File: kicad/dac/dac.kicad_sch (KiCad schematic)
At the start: 41 parts, among them J1 USB_C_Receptacle_USB2.0, J2 Conn_01x03, J3 Conn_01x03, J4 AudioJack3, P1 Conn_WallPlug_Earth, T1 Transformer_SP_2S, U2 PCM2704/4C/5/5C, Y1 12MHz±0.05%

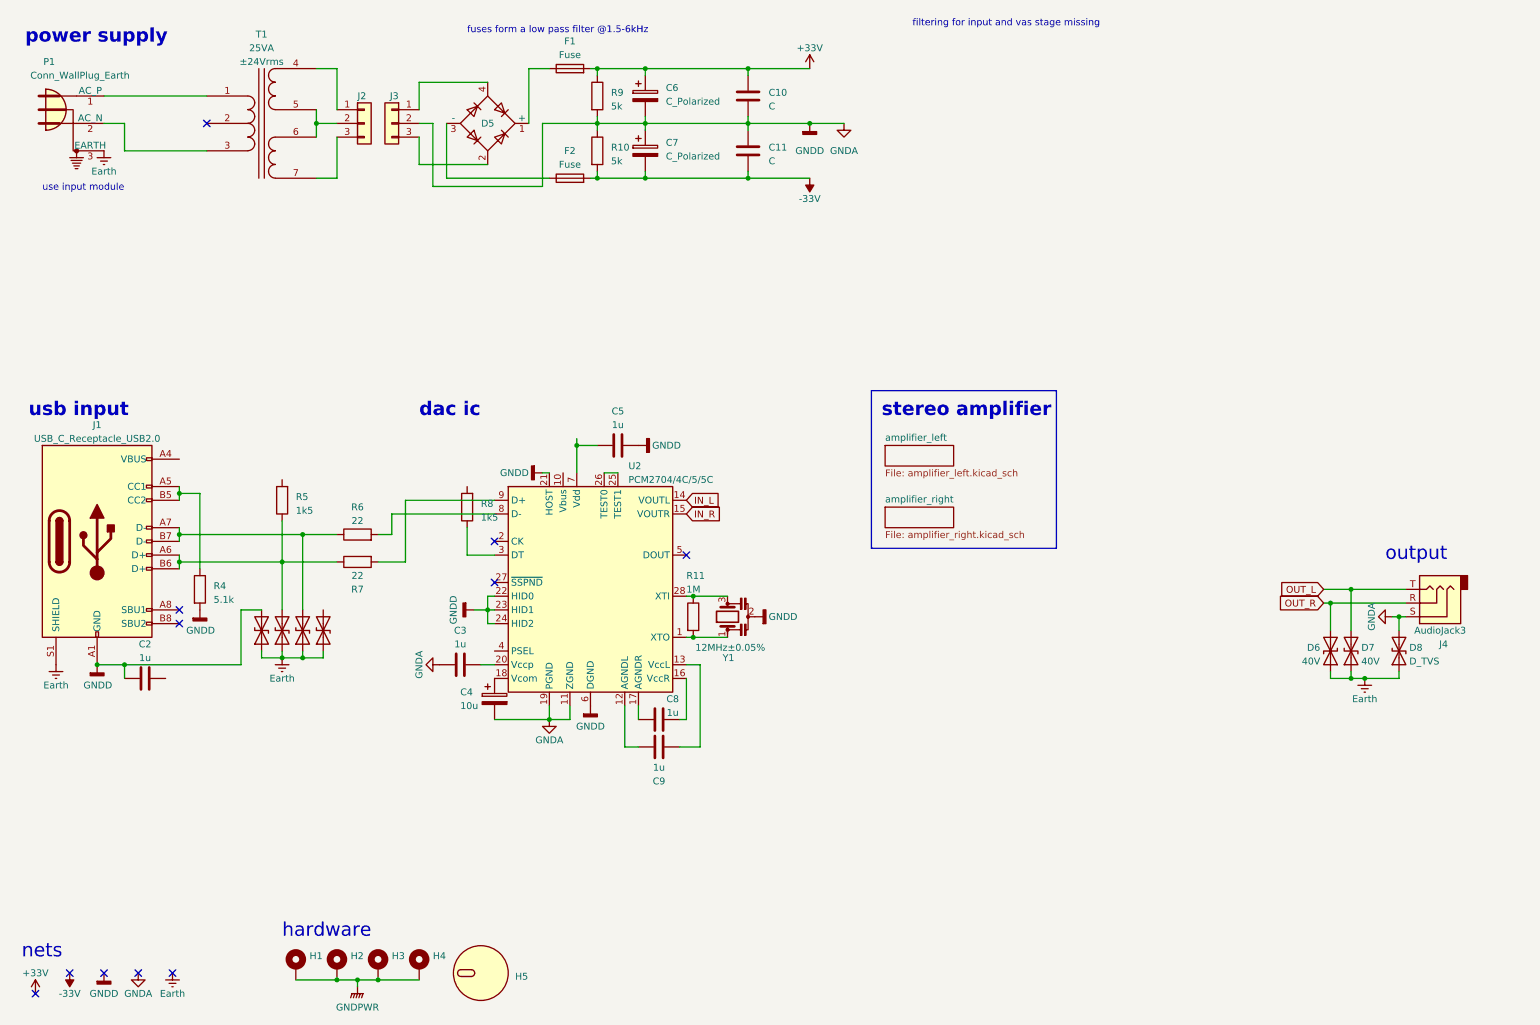
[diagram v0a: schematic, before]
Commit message: split power supply to different board
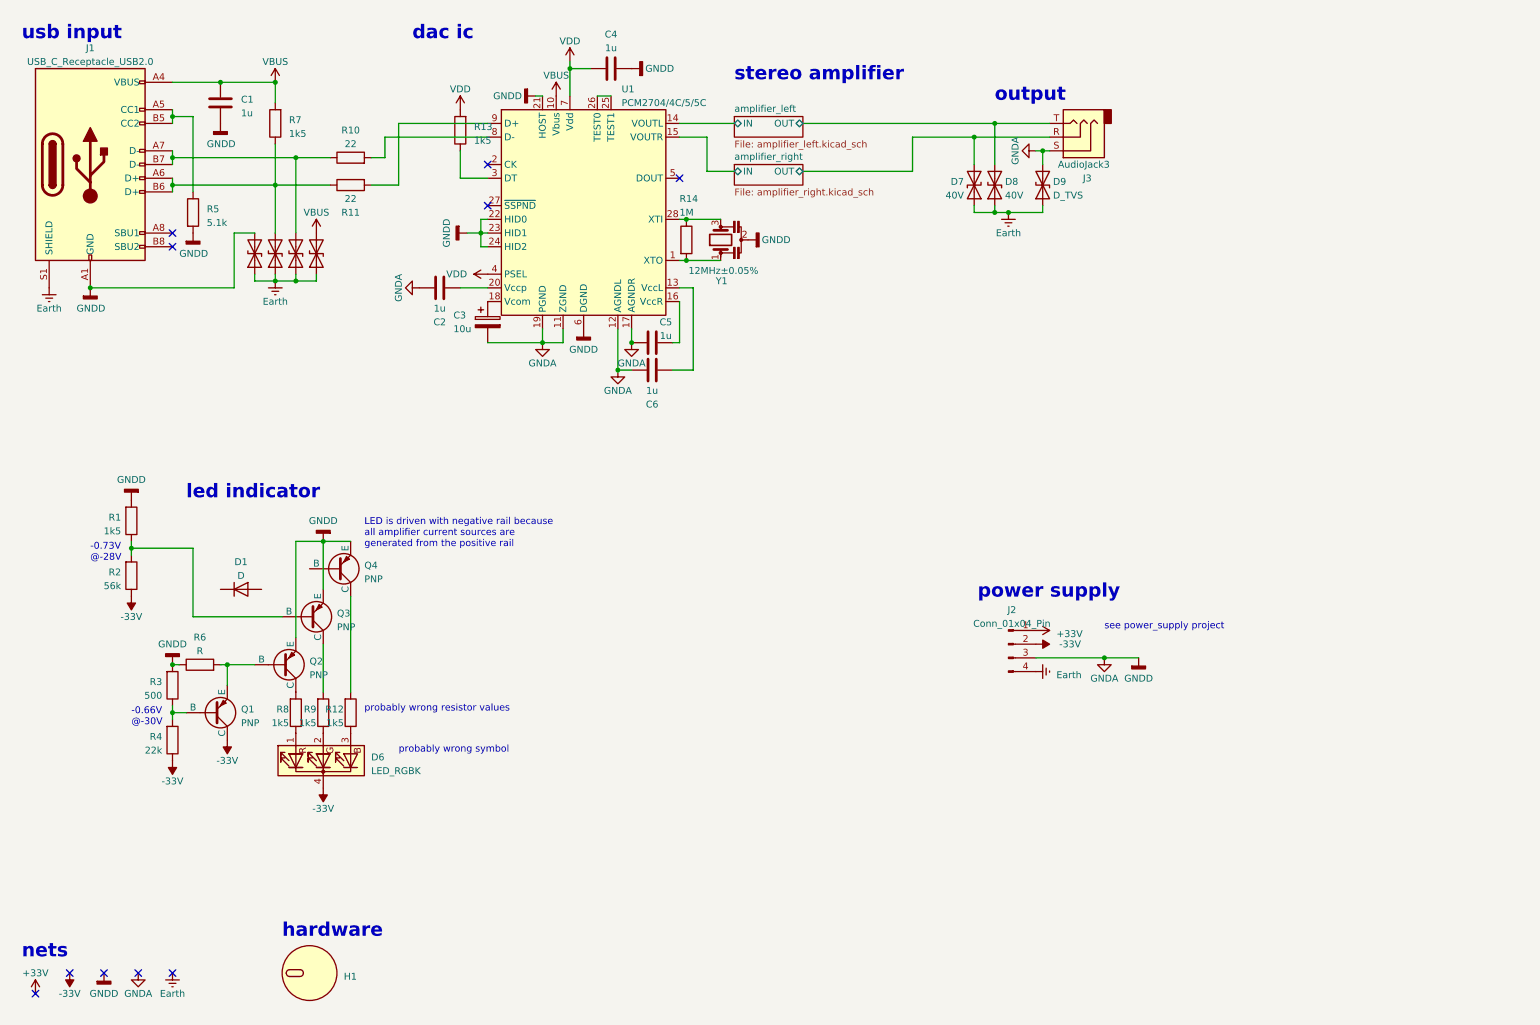
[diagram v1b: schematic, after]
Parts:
- removed C10, C11: C, symbol Device:C
- removed C6, C7: C_Polarized, symbol Device:C_Polarized
- removed D5: ~, symbol Diode_Bridge:KBPC1501T
- removed F1, F2: Fuse, symbol Device:Fuse
- removed H1, H2, H3, H4: MountingHole_Pad, symbol Mechanical:MountingHole_Pad
- removed J2, J3: Conn_01x03, symbol Connector_Generic:Conn_01x03
- removed P1: Conn_WallPlug_Earth, symbol Connector:Conn_WallPlug_Earth
- removed R10: 5k, Resistor_THT:R_Axial_DIN0207_L6.3mm_D2.5mm_P10.16mm_Horizontal, symbol Device:R
- removed T1: Transformer_SP_2S, symbol Device:Transformer_SP_2S
- added D1: D, symbol Device:D
- added D6: LED_RGBK, symbol Device:LED_RGBK
- added J2: Conn_01x04_Pin, symbol Connector:Conn_01x04_Pin
- added Q1, Q2, Q3, Q4: PNP, Package_TO_SOT_THT:TO-92L_Inline, symbol Simulation_SPICE:PNP
- added R1, R12, R8: 1k5, Resistor_SMD:R_0805_2012Metric_Pad1.20x1.40mm_HandSolder, symbol Device:R
- added R2: 56k, Resistor_SMD:R_0805_2012Metric_Pad1.20x1.40mm_HandSolder, symbol Device:R
- added R3: 500, Resistor_SMD:R_0805_2012Metric_Pad1.20x1.40mm_HandSolder, symbol Device:R
- added R4: 22k, Resistor_SMD:R_0805_2012Metric_Pad1.20x1.40mm_HandSolder, symbol Device:R
- added R6: R, Resistor_SMD:R_0805_2012Metric_Pad1.20x1.40mm_HandSolder, symbol Device:R
- R9: value 5k -> 1k5; footprint Resistor_THT:R_Axial_DIN0207_L6.3mm_D2.5mm_P10.16mm_Horizontal -> Resistor_SMD:R_0805_2012Metric_Pad1.20x1.40mm_HandSolder
- renumbered C2 to C1, C3 to C2, C4 to C3, C5 to C4, C8 to C5, C9 to C6, D1 to D2, D2 to D3, D3 to D4, D4 to D5, D6 to D7, D7 to D8, D8 to D9, H5 to H1, J4 to J3, R6 to R10, R7 to R11, R8 to R13, R11 to R14, R4 to R5, R5 to R7, U2 to U1
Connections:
- net +36V: now also J2.1 (Pin_1); no longer R9.1
- net -36V: now also D6.4 (K), J2.2 (Pin_2), Q1.1 (C), R2.1, R4.1
- net Earth: now also J2.4 (Pin_4)
- net GNDA: now also C5.1, C6.1, U1.12 (AGNDL), U1.17 (AGNDR), J2.3 (Pin_3), Q2.3 (E), Q3.3 (E), Q4.3 (E), R1.2, R3.2, R6.1; no longer R9.2
- net VBUS: now reaches D5.2 (A2)
- net VBUS: now also C1.2, J1.A4 (VBUS), J1.A9 (VBUS), J1.B4 (VBUS), J1.B9 (VBUS), R7.2, U1.10 (Vbus)
- net VDD: now reaches R13.2
- net VDD: now also C4.1, U1.4 (PSEL), U1.7 (Vdd)
- net IN_L renamed amplifier_left/IN
- net IN_R renamed amplifier_right/IN
- net OUT_L renamed amplifier_left/OUT
- net OUT_R renamed amplifier_right/OUT
- new net: Q2.1 (C), R8.2
- new net: Q1.3 (E), Q2.2 (B), R6.2
- new net: Q1.2 (B), R3.1, R4.2
- new net: D6.1 (RA), R8.1
- new net: Q3.2 (B), R1.1, R2.2
- new net: D6.2 (GA), R9.1
- new net: D6.3 (BA), R12.1
- new net: Q3.1 (C), R9.2
- new net: Q4.1 (C), R12.2
- no-connect marks 11 -> 10
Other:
- sheet amplifier_left ports: added IN, OUT; removed none
- sheet amplifier_right ports: added IN, OUT; removed none
- note added: "-0.66V @-30V"
- note added: "-0.73V @-28V"
- note added: "LED is driven with negative rail because all amplifier current sources are generated from the positive rail"
- note added: "led indicator"
- note added: "probably wrong resistor values"
- note added: "probably wrong symbol"
- note added: "see power_supply project"
- note removed: "filtering for input and vas stage missing"
- note removed: "fuses form a low pass filter @1.5-6kHz"
- note removed: "use input module"
- moved on the sheet: C1, C2, C3, C4, C5, C6, D7, D8, D9, H1, J1, J3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

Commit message: Commit
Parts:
- removed C1, C4, C6: 1u, Capacitor_SMD:C_0805_2012Metric_Pad1.18x1.45mm_HandSolder, symbol Device:C
- removed C3: 10u, symbol Device:C_Polarized
- removed D2, D3, D4, D5, D9: D_TVS, symbol Device:D_TVS
- removed D7, D8: 40V, symbol Device:D_TVS
- removed J1: USB_C_Receptacle_USB2.0, Connector_USB:USB_C_Receptacle_GCT_USB4085, symbol Connector:USB_C_Receptacle_USB2.0
- removed J2: Conn_01x04_Pin, symbol Connector:Conn_01x04_Pin
- removed R14: 1M, Resistor_SMD:R_0805_2012Metric_Pad1.20x1.40mm_HandSolder, symbol Device:R
- removed U1: PCM2704/4C/5/5C, Package_SO:SSOP-28_5.3x10.2mm_P0.65mm, symbol library:PCM2704/4C/5/5C
- removed Y1: 12MHz±0.05%, symbol Device:Resonator
- added C1, C4, C6, C9: 10u, symbol Device:C_Polarized
- added C10, C7: 100n, Capacitor_SMD:C_1206_3216Metric_Pad1.33x1.80mm_HandSolder, symbol Device:C
- added C11, C12: 10u, symbol Device:C
- added C13, C14: 20n, Capacitor_SMD:C_1206_3216Metric_Pad1.33x1.80mm_HandSolder, symbol Device:C
- added C15, C16: 10u, Capacitor_SMD:C_1206_3216Metric_Pad1.33x1.80mm_HandSolder, symbol Device:C
- added C3, C8: 2u2, Capacitor_SMD:C_1206_3216Metric_Pad1.33x1.80mm_HandSolder, symbol Device:C
- added D1, D10, D11, D12, D13, D14, D15, D2, D3, D4, D5, D6, D7, D8, D9: D, symbol Device:D
- added J2: AudioJack3_SwitchT, symbol Connector_Audio:AudioJack3_SwitchT
- added J3: Conn_01x09_Pin, Connector_PinHeader_2.54mm:PinHeader_1x09_P2.54mm_Vertical, symbol Connector:Conn_01x09_Pin
- added J3: AudioJack3_SwitchTR, symbol Connector_Audio:AudioJack3_SwitchTR
- added K1: Relay, symbol Relay:EC2-3NU
- added N1: Housing, symbol Mechanical:Housing
- added Q1: NPN, symbol Simulation_SPICE:NPN
- added Q2, Q3: PNP, symbol Simulation_SPICE:PNP
- added R1, R2: 100k, symbol Device:R
- added R12: 5k1, Resistor_SMD:R_1206_3216Metric_Pad1.30x1.75mm_HandSolder, symbol Device:R
- added R3, R4, R8, R9: 16, Resistor_SMD:R_1206_3216Metric_Pad1.30x1.75mm_HandSolder, symbol Device:R
- added R6: 10k, symbol Device:R
- added U1: PCM510xA, Package_SO:TSSOP-20_4.4x6.5mm_P0.65mm, symbol library:PCM510xA
- C2: value 1u -> 100n; footprint Capacitor_SMD:C_0805_2012Metric_Pad1.18x1.45mm_HandSolder -> Capacitor_SMD:C_1206_3216Metric_Pad1.33x1.80mm_HandSolder
- C5: value 1u -> 2u2; footprint Capacitor_SMD:C_0805_2012Metric_Pad1.18x1.45mm_HandSolder -> Capacitor_SMD:C_1206_3216Metric_Pad1.33x1.80mm_HandSolder
- J4: renamed from J3; symbol Connector_Audio:AudioJack3 -> Connector_Audio:AudioJack3_Switch; Digikey 889-1818-ND -> 2223-SJ-63073E-ND
- Q4: renamed from Q1; footprint Package_TO_SOT_THT:TO-92L_Inline -> Package_TO_SOT_THT:TO-92
- Q5: renamed from Q2; footprint Package_TO_SOT_THT:TO-92L_Inline -> Package_TO_SOT_THT:TO-92
- Q6: renamed from Q3; footprint Package_TO_SOT_THT:TO-92L_Inline -> Package_TO_SOT_THT:TO-92
- Q7: renamed from Q4; footprint Package_TO_SOT_THT:TO-92L_Inline -> Package_TO_SOT_THT:TO-92
- R10, R11: value 22 -> 2; footprint Resistor_SMD:R_0805_2012Metric_Pad1.20x1.40mm_HandSolder -> Resistor_SMD:R_1206_3216Metric_Pad1.30x1.75mm_HandSolder
- R13: value 1k5 -> 5k1; footprint Resistor_SMD:R_0805_2012Metric_Pad1.20x1.40mm_HandSolder -> Resistor_SMD:R_1206_3216Metric_Pad1.30x1.75mm_HandSolder
- R14: renamed from R1; footprint Resistor_SMD:R_0805_2012Metric_Pad1.20x1.40mm_HandSolder -> Resistor_SMD:R_1206_3216Metric_Pad1.30x1.75mm_HandSolder
- R15: renamed from R2; footprint Resistor_SMD:R_0805_2012Metric_Pad1.20x1.40mm_HandSolder -> Resistor_SMD:R_1206_3216Metric_Pad1.30x1.75mm_HandSolder
- R16: renamed from R3; footprint Resistor_SMD:R_0805_2012Metric_Pad1.20x1.40mm_HandSolder -> Resistor_SMD:R_1206_3216Metric_Pad1.30x1.75mm_HandSolder
- R17: renamed from R4; footprint Resistor_SMD:R_0805_2012Metric_Pad1.20x1.40mm_HandSolder -> Resistor_SMD:R_1206_3216Metric_Pad1.30x1.75mm_HandSolder
- R18: renamed from R6; footprint Resistor_SMD:R_0805_2012Metric_Pad1.20x1.40mm_HandSolder -> Resistor_SMD:R_1206_3216Metric_Pad1.30x1.75mm_HandSolder
- R19: renamed from R8; footprint Resistor_SMD:R_0805_2012Metric_Pad1.20x1.40mm_HandSolder -> Resistor_SMD:R_1206_3216Metric_Pad1.30x1.75mm_HandSolder
- R20: renamed from R9; footprint Resistor_SMD:R_0805_2012Metric_Pad1.20x1.40mm_HandSolder -> Resistor_SMD:R_1206_3216Metric_Pad1.30x1.75mm_HandSolder
- R21: renamed from R12; footprint Resistor_SMD:R_0805_2012Metric_Pad1.20x1.40mm_HandSolder -> Resistor_SMD:R_1206_3216Metric_Pad1.30x1.75mm_HandSolder
- R5: value 5.1k -> 100k; footprint Resistor_SMD:R_0805_2012Metric_Pad1.20x1.40mm_HandSolder -> (none)
- R7: value 1k5 -> R; footprint Resistor_SMD:R_0805_2012Metric_Pad1.20x1.40mm_HandSolder -> (none)
- renumbered D1 to D16, D6 to D17
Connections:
- net VDD is gone; now on net OUT_R: R13.2
- net GNDA: now also R13.1, C1.2, C10.2, C11.2, C12.2, C13.1, C14.1, C3.2, C4.2, C6.2, C7.1, C9.2, D5.1 (K), D6.2 (A), J2.S, J3.3 (Pin_3), J3.S, R12.1, R8.2, R9.2, U1.10 (DEMP), U1.11 (FLT), U1.16 (FMT), U1.19 (DGND), U1.3 (CPGND), U1.9 (AGND); no longer J4.S, R5.2
- net at C5.2: now also U1.5 (VNEG)
- net at C2.2: now also C1.1, U1.18 (LDOO)
- net at R7.1: now also Q2.3 (E); no longer R11.1
- net OUT_R: now reaches R11.2
- net OUT_R: now also D14.2 (A), D15.1 (K), J2.R, J3.R, K1.4
- net at R10.1: now also C15.2
- net OUT_L: now reaches R10.2
- net OUT_L: now also D12.2 (A), D13.1 (K), J2.T, J3.T, K1.9, R12.2
- net -36V renamed -30V
- net -30V: now also D10.2 (A), D13.2 (A), D15.2 (A), D8.2 (A), J3.2 (Pin_2)
- net VBUS: no longer names the net of R7.2
- net amplifier_left/OUT: no longer names the net of J4.T
- net amplifier_right/OUT: no longer names the net of J4.R
- new net: C10.1, C9.1, U1.8 (AVDD)
- new net: C11.1, D1.2 (A), D2.1 (K), R1.2
- new net: Q1.1 (C), R6.2
- new net: D1.1 (K), D3.1 (K), D6.1 (K), Q1.2 (B)
- new net: Q1.3 (E), Q2.1 (C)
- new net: Q3.2 (B), R5.2, R6.1
- new net: C13.2, R3.1
- new net: C8.1, U1.2 (CAPP)
- new net: C8.2, U1.4 (CAPM)
- new net: D2.2 (A), D4.2 (A), D5.2 (A), Q2.2 (B)
- new net: C3.1, C4.1, U1.1 (CPVDD)
- new net: D11.1 (K), K1.1
- new net: D11.2 (A), K1.12
- new net: C16.2, R11.1
- new net: C12.1, D3.2 (A), D4.1 (K), R2.2
- new net: C14.2, R4.1
- new net: K1.10, R8.1
- new net: K1.3, R9.1
- new net +30V: D12.1 (K), D14.1 (K), D7.1 (K), D9.1 (K), J3.1 (Pin_1)
- new net +3V3: C6.1, C7.2, J3.4 (Pin_4), U1.20 (DVDD)
- new net AMP_L: C15.1, D7.2 (A), D8.1 (K), K1.8, R3.2
- new net AMP_R: C16.1, D10.1 (K), D9.2 (A), K1.5, R4.2
- new net BCK: J3.6 (Pin_6), U1.13 (BCK)
- new net DAC_L: U1.6 (OUTL)
- new net DAC_R: U1.7 (OUTR)
- new net DATA: J3.8 (Pin_8), U1.14 (DIN)
- new net LRCK: J3.5 (Pin_5), U1.15 (LRCK)
- new net SCK: J3.7 (Pin_7), U1.12 (SCK)
- new net SSPND: J3.9 (Pin_9), U1.17 (XSMT)
- no-connect marks 10 -> 9
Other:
- note added: "Cr = red || yellow Cg = green && ~blue && ~red Cb = blue && green"
- note added: "DAC IC"
- note added: "Hardware"
- note added: "LED Indicator"
- note added: "Output Protection"
- note added: "Power Supply"
- note added: "Stereo Amplifier"
- note added: "or gate"
- note removed: "dac ic"
- note removed: "hardware"
- note removed: "led indicator"
- note removed: "nets"
- note removed: "output"
- note removed: "power supply"
- note removed: "stereo amplifier"
- note removed: "usb input"
- moved on the sheet: D16, D17, H1, Q4, Q5, Q6, Q7, R14, R15, R16, R17, R18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
